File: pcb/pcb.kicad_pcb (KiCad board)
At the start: 4 copper layers, 41.8 x 39.9 mm, 79 parts, among them J1 Conn_ARM_SWD_TagConnect_TC2030, J2 USB_C_Receptacle_USB2.0_16P, J3 C-OBD-II-16M, J4 GND_Connect, J5 Conn_ARM_SWD_TagConnect_TC203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, SW1 RESET_BUTTON, U1 STM32G431KBTx, U2 USBLC6-2SC6, U3 FT230XS, U4 SPX3819M5-L, U5 LM66100DCK, U6 TCAN337, U7 LM2842X, U8 LM66100DCK, U9 BLUENRG-M2SP, Y1 830103622909

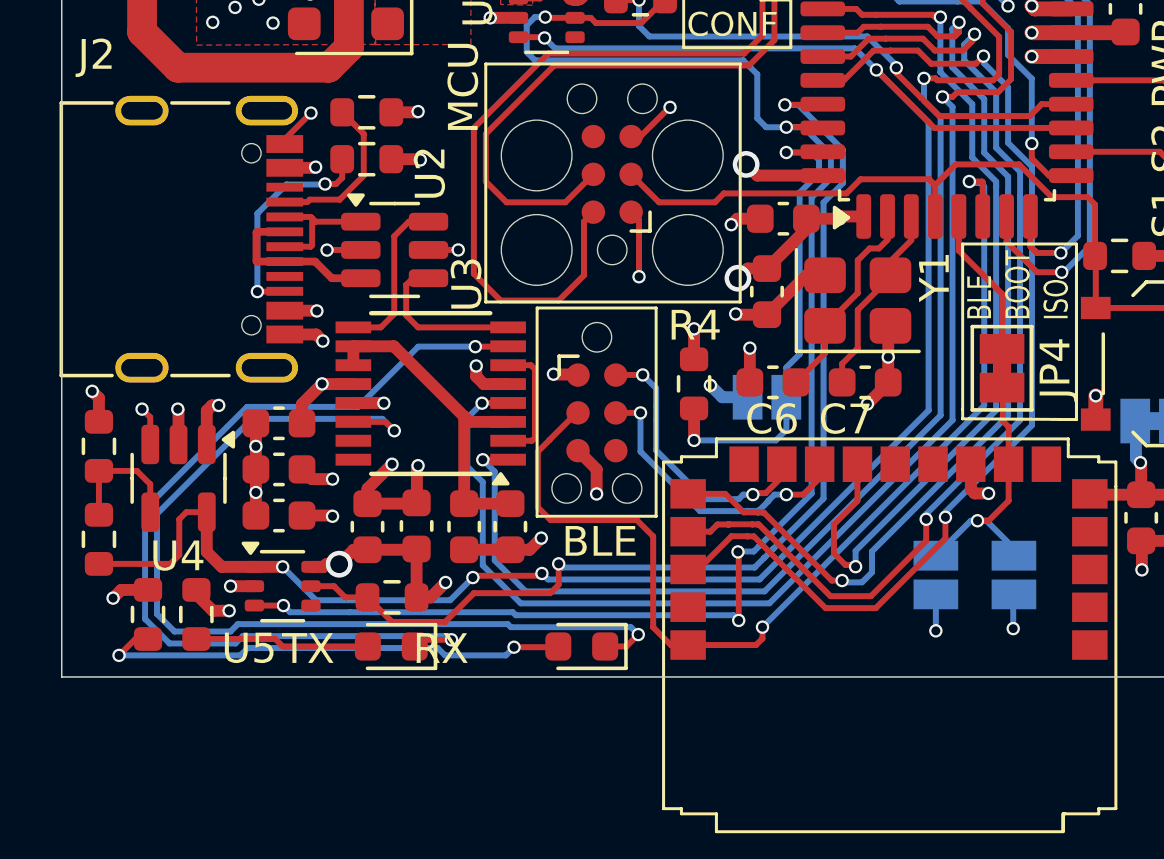
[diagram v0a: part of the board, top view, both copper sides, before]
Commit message: add slot for filter
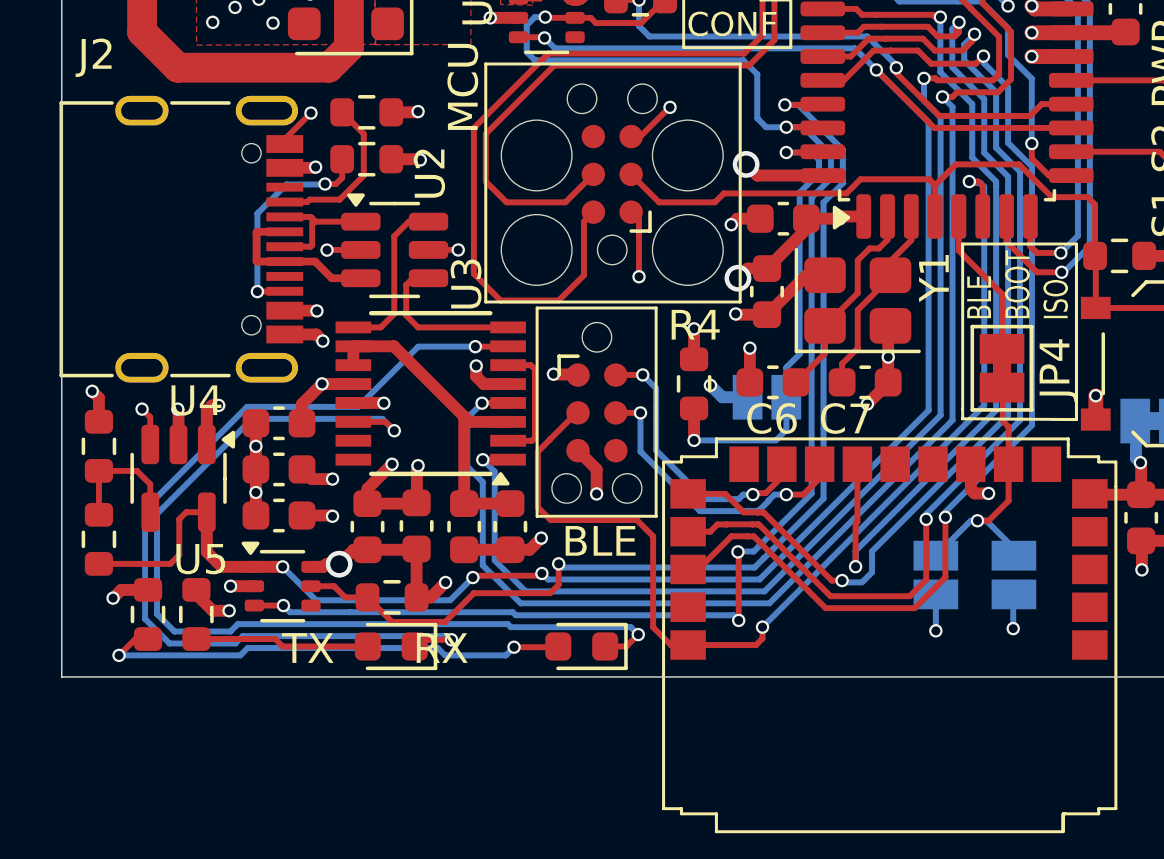
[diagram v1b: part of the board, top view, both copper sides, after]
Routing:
- net /ble/SPI_MOSI: track 35.3 -> 36.0 mm
- net /ble/SPI_MISO: track 35.0 -> 35.7 mm
- net /SPI_CS: track 29.5 -> 28.8 mm

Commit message: update
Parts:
- added G1: LOGO, custom:logo, F.Cu at (143.5, 116.0)
- J1: value Conn_ARM_SWD_TagConnect_TC2030 -> Conn_ARM_SWD_TagConnect_TC2030-NL; footprint Connector:Tag-Connect_TC2030-IDC-FP_2x03_P1.27mm_Vertical -> Connector:Tag-Connect_TC2030-IDC-NL_2x03_P1.27mm_Vertical
- moved J1 2.63 mm to (146.5, 111.5), turned to 0 degrees
- moved J5 1.49 mm to (144.0, 122.8)
- moved R10 0.25 mm to (128.9, 128.3)
- moved R11 0.25 mm to (130.5, 128.3)
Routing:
- net /T_JTMS_SWDIO: track 31.3 -> 13.9 mm
- net /T_JCLK_SWCLK: track 23.9 -> 11.5 mm
- net /usb/RXLED: track 32.3 -> 23.5 mm
- net /usb/TXLED: track 30.3 -> 22.4 mm
- net GND: track 85.5 -> 88.4 mm, vias 73 -> 72
- net /ble/BLE_SWDIO: track 9.29 -> 7.75 mm
- net /ble/BLE_SWCLK: track 9.95 -> 8.55 mm
- net /BLE_NRST: track 35.4 -> 34.1 mm, vias 2 -> 4
- net /SYS_NRST: track 27.8 -> 27.1 mm, vias 0 -> 2
- net +3V3: track 50.2 -> 50.8 mm, vias 23 -> 22
- net Net-(DS5-A): track 5.87 -> 6.01 mm, vias 0 -> 2
